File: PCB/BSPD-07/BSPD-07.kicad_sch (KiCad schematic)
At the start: 54 parts, among them IC1 LM393LVQDRQ1, IC2 LM393LVQDRQ1, IC3 LM393LVQDRQ1, IC4 LDO40LPU50RY, IC5 74LVC1G02GW-Q100H, J1 DTM13-12PA, Q1 RSQ025P03HZGTR, Q2 RJU002N06FRAT106, Q3 RJU002N06FRAT106, U2 TLP175A / COMUS AB38-Q

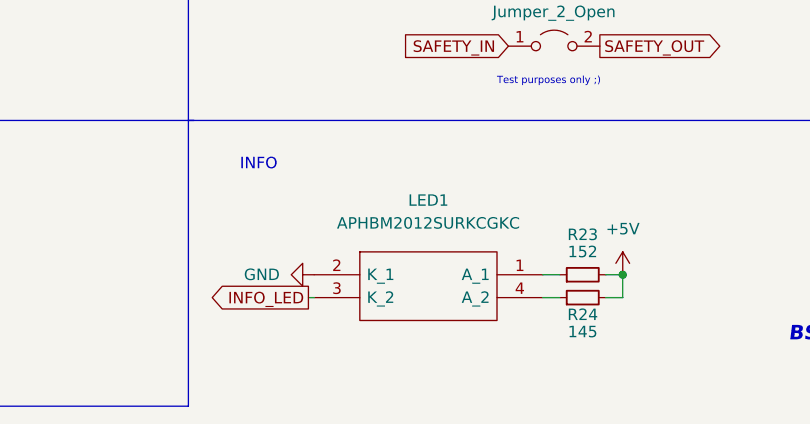
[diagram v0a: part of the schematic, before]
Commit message: Layout rework + led change
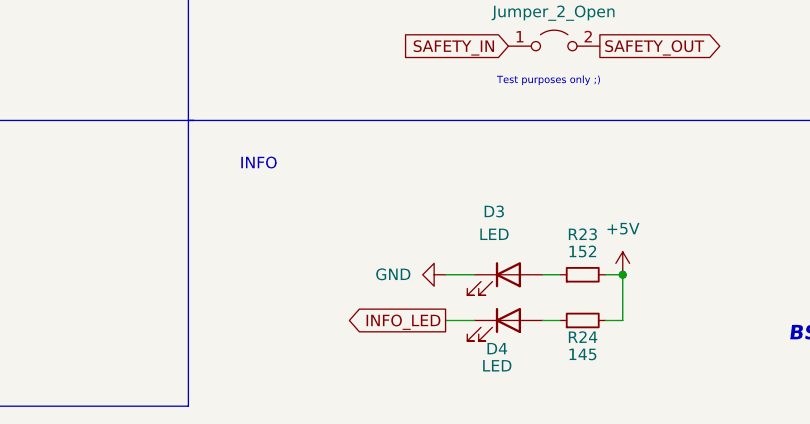
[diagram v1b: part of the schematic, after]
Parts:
- removed LED1: APHBM2012SURKCGKC, BSPD_07:APHBM2012SURKCGKC, symbol BSPD-07:APHBM2012SURKCGKC
- added D3, D4: LED, Diode_SMD:D_0402_1005Metric_Pad0.77x0.64mm_HandSolder, symbol Device:LED
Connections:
- net GND: now also D3.1 (K)
- net INFO_LED: now also D4.1 (K)
- net at R24.1: now also D4.2 (A)
- net at R23.1: now also D3.2 (A)
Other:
- moved on the sheet: R24
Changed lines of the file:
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@@
+    (stroke (width 0) (type default) (color 0 0 0 0))
+  )
+  (wire (pts (xy 159.385 188.595) (xy 161.29 188.595))
     (stroke (width 0) (type default) (color 0 0 0 0))
   )
@@
     (stroke (width 0) (type default) (color 0 0 0 0))
   )
-  (wire (pts (xy 159.385 186.055) (xy 161.29 186.055))
-    (stroke (width 0) (type default) (color 0 0 0 0))
-  )
   (polyline (pts (xy 193.675 52.705) (xy 150.495 52.705))
     (stroke (width 0) (type default) (color 0 0 0 0))
@@
     (stroke (width 0) (type default) (color 0 0 0 0))
   )
+  (wire (pts (xy 148.59 188.595) (xy 151.765 188.595))
+    (stroke (width 0) (type default) (color 0 0 0 0))
+  )
   (wire (pts (xy 159.385 139.065) (xy 159.385 140.335))
     (stroke (width 0) (type default) (color 0 0 0 0))
@@
     (stroke (width 0) (type default) (color 0 0 0 0))
   )
-  (wire (pts (xy 133.35 186.055) (xy 133.985 186.055))
-    (stroke (width 0) (type default) (color 0 0 0 0))
-  )
   (wire (pts (xy 57.785 107.95) (xy 59.69 107.95))
     (stroke (width 0) (type default) (color 0 0 0 0))
@@
     (stroke (width 0) (type default) (color 0 0 0 0))
   )
+  (wire (pts (xy 168.275 188.595) (xy 166.37 188.595))
+    (stroke (width 0) (type default) (color 0 0 0 0))
+  )
   (wire (pts (xy 263.525 120.65) (xy 263.525 123.19))
     (stroke (width 0) (type default) (color 0 0 0 0))
@@
     (stroke (width 0) (type default) (color 0 0 0 0))
   )
-  (wire (pts (xy 168.275 186.055) (xy 168.275 183.515))
+  (wire (pts (xy 168.275 183.515) (xy 168.275 188.595))
     (stroke (width 0) (type default) (color 0 0 0 0))
   )
@@
     (stroke (width 0) (type default) (color 0 0 0 0))
   )
+  (wire (pts (xy 148.59 183.515) (xy 151.765 183.515))
+    (stroke (width 0) (type default) (color 0 0 0 0))
+  )
   (wire (pts (xy 50.8 33.02) (xy 50.8 38.1))
     (stroke (width 0) (type default) (color 0 0 0 0))
@@
   )
   (wire (pts (xy 220.98 47.625) (xy 220.98 52.07))
-    (stroke (width 0) (type default) (color 0 0 0 0))
-  )
-  (wire (pts (xy 166.37 186.055) (xy 168.275 186.055))
     (stroke (width 0) (type default) (color 0 0 0 0))
   )
@@
     )
   )
-  (global_label "INFO_LED" (shape output) (at 133.35 186.055 180) (fields_autoplaced)
+  (global_label "INFO_LED" (shape output) (at 148.59 188.595 180) (fields_autoplaced)
     (effects (font (size 1.27 1.27)) (justify right))
-    (property "Intersheet References" "${INTERSHEET_REFS}" (id 0) (at 122.1679 185.9756 0)
+    (property "Intersheet References" "${INTERSHEET_REFS}" (id 0) (at 137.4079 188.5156 0)
       (effects (font (size 1.27 1.27)) (justify right) hide)
     )
@@
     (pin "1")
   )
-  (symbol (lib_id "Device:R_Small") (at 163.83 186.055 90) (unit 1)
-    (in_bom yes) (on_board yes)
-    (property "Reference" "R24" (id 0) (at 163.83 187.96 90))
-    (property "Value" "145" (id 1) (at 163.83 189.865 90))
-    (property "Footprint" "Resistor_SMD:R_0402_1005Metric" (id 2) (at 163.83 186.055 0)
-      (effects (font (size 1.27 1.27)) hide)
-    )
-    (property "Datasheet" "~" (id 3) (at 163.83 186.055 0)
+  (symbol (lib_id "Device:R_Small") (at 163.83 188.595 90) (unit 1)
+    (in_bom yes) (on_board yes)
+    (property "Reference" "R24" (id 0) (at 163.83 190.5 90))
+    (property "Value" "145" (id 1) (at 163.83 192.405 90))
+    (property "Footprint" "Resistor_SMD:R_0402_1005Metric" (id 2) (at 163.83 188.595 0)
+      (effects (font (size 1.27 1.27)) hide)
+    )
+    (property "Datasheet" "~" (id 3) (at 163.83 188.595 0)
       (effects (font (size 1.27 1.27)) hide)
     )
@@
     (pin "1")
     (pin "2")
-  )
-  (symbol (lib_id "BSPD-07:APHBM2012SURKCGKC") (at 133.985 183.515 0) (unit 1)
-    (in_bom yes) (on_board yes) (fields_autoplaced)
-    (property "Reference" "LED1" (id 0) (at 146.685 175.26 0))
-    (property "Value" "APHBM2012SURKCGKC" (id 1) (at 146.685 177.8 0))
-    (property "Footprint" "BSPD_07:APHBM2012SURKCGKC" (id 2) (at 155.575 180.975 0)
-      (effects (font (size 1.27 1.27)) (justify left) hide)
-    )
-    (property "Datasheet" "https://mouser.componentsearchengine.com/Datasheets/3/APHBM2012SURKCGKC.pdf" (id 3) (at 155.575 183.515 0)
-      (effects (font (size 1.27 1.27)) (justify left) hide)
-    )
-    (property "Description" "2.0X1.2MM RED/GREEN SMD LED Kingbright APHBM2012SURKCGKC, APHBM2012 Series Bi-colour Green, Red LED, 570 / 630 nm 4-Pin 2012 (0805) Clear" (id 4) (at 155.575 186.055 0)
-      (effects (font (size 1.27 1.27)) (justify left) hide)
-    )
-    (property "Height" "0.45" (id 5) (at 155.575 188.595 0)
-      (effects (font (size 1.27 1.27)) (justify left) hide)
-    )
-    (property "Manufacturer_Name" "Kingbright" (id 6) (at 155.575 191.135 0)
-      (effects (font (size 1.27 1.27)) (justify left) hide)
-    )
-    (property "Manufacturer_Part_Number" "APHBM2012SURKCGKC" (id 7) (at 155.575 193.675 0)
-      (effects (font (size 1.27 1.27)) (justify left) hide)
-    )
-    (property "Mouser Part Number" "604-BM2012SURKCGKC" (id 8) (at 155.575 196.215 0)
-      (effects (font (size 1.27 1.27)) (justify left) hide)
-    )
-    (property "Mouser Price/Stock" "https://www.mouser.co.uk/ProductDetail/Kingbright/APHBM2012SURKCGKC?qs=mWUXtl%252BhaIKZSpp3TSJ%2FQA%3D%3D" (id 9) (at 155.575 198.755 0)
-      (effects (font (size 1.27 1.27)) (justify left) hide)
-    )
-    (property "Arrow Part Number" "APHBM2012SURKCGKC" (id 10) (at 155.575 201.295 0)
-      (effects (font (size 1.27 1.27)) (justify left) hide)
-    )
-    (property "Arrow Price/Stock" "https://www.arrow.com/en/products/aphbm2012surkcgkc/kingbright?region=nac" (id 11) (at 155.575 203.835 0)
-      (effects (font (size 1.27 1.27)) (justify left) hide)
-    )
-    (property "Mouser Testing Part Number" "" (id 12) (at 155.575 206.375 0)
-      (effects (font (size 1.27 1.27)) (justify left) hide)
-    )
-    (property "Mouser Testing Price/Stock" "" (id 13) (at 155.575 208.915 0)
-      (effects (font (size 1.27 1.27)) (justify left) hide)
-    )
-    (pin "1")
-    (pin "2")
-    (pin "3")
-    (pin "4")
   )
   (symbol (lib_id "power:+5V") (at 213.995 36.195 270) (unit 1)
@@
     (pin "3")
   )
+  (symbol (lib_id "Device:LED") (at 155.575 188.595 0) (unit 1)
+    (in_bom yes) (on_board yes)
+    (property "Reference" "D4" (id 0) (at 154.305 191.77 0))
+    (property "Value" "LED" (id 1) (at 154.305 193.675 0))
+    (property "Footprint" "Diode_SMD:D_0402_1005Metric_Pad0.77x0.64mm_HandSolder" (id 2) (at 155.575 188.595 0)
+      (effects (font (size 1.27 1.27)) hide)
+    )
+    (property "Datasheet" "~" (id 3) (at 155.575 188.595 0)
+      (effects (font (size 1.27 1.27)) hide)
+    )
+    (pin "1")
+    (pin "2")
+  )
   (symbol (lib_id "BSPD-07:74LVC1G02GW-Q100H") (at 49.53 146.05 0) (unit 1)
     (in_bom yes) (on_board yes) (fields_autoplaced)
@@
     (pin "1")
   )
-  (symbol (lib_id "power:GND") (at 133.985 183.515 270) (unit 1)
-    (in_bom yes) (on_board yes) (fields_autoplaced)
-    (property "Reference" "#PWR0147" (id 0) (at 127.635 183.515 0)
-      (effects (font (size 1.27 1.27)) hide)
-    )
-    (property "Value" "GND" (id 1) (at 130.175 183.5149 90)
+  (symbol (lib_id "power:GND") (at 148.59 183.515 270) (unit 1)
+    (in_bom yes) (on_board yes) (fields_autoplaced)
+    (property "Reference" "#PWR0147" (id 0) (at 142.24 183.515 0)
+      (effects (font (size 1.27 1.27)) hide)
+    )
+    (property "Value" "GND" (id 1) (at 144.78 183.5149 90)
       (effects (font (size 1.27 1.27)) (justify right))
     )
-    (property "Footprint" "" (id 2) (at 133.985 183.515 0)
-      (effects (font (size 1.27 1.27)) hide)
-    )
-    (property "Datasheet" "" (id 3) (at 133.985 183.515 0)
+    (property "Footprint" "" (id 2) (at 148.59 183.515 0)
+      (effects (font (size 1.27 1.27)) hide)
+    )
+    (property "Datasheet" "" (id 3) (at 148.59 183.515 0)
       (effects (font (size 1.27 1.27)) hide)
     )
@@
     (pin "2")
   )
+  (symbol (lib_id "Device:LED") (at 155.575 183.515 0) (unit 1)
+    (in_bom yes) (on_board yes) (fields_autoplaced)
+    (property "Reference" "D3" (id 0) (at 153.9875 176.53 0))
+    (property "Value" "LED" (id 1) (at 153.9875 179.07 0))
+    (property "Footprint" "Diode_SMD:D_0402_1005Metric_Pad0.77x0.64mm_HandSolder" (id 2) (at 155.575 183.515 0)
+      (effects (font (size 1.27 1.27)) hide)
+    )
+    (property "Datasheet" "~" (id 3) (at 155.575 183.515 0)
+      (effects (font (size 1.27 1.27)) hide)
+    )
+    (pin "1")
+    (pin "2")
+  )
   (symbol (lib_id "Device:R_Small") (at 218.44 50.8 0) (unit 1)
     (in_bom yes) (on_board yes)
@@
       (reference "D2") (unit 1) (value "7V") (footprint "Diode_SMD:D_0402_1005Metric")
     )
+    (path "/ceeae0f3-eeb4-4e60-9d26-30190a673d37"
+      (reference "D3") (unit 1) (value "LED") (footprint "Diode_SMD:D_0402_1005Metric_Pad0.77x0.64mm_HandSolder")
+    )
+    (path "/8f4dccc8-5830-44b2-a241-6731b10d74d3"
+      (reference "D4") (unit 1) (value "LED") (footprint "Diode_SMD:D_0402_1005Metric_Pad0.77x0.64mm_HandSolder")
+    )
     (path "/90a442e5-8955-4be7-a2a2-5ce96ee123ec"
       (reference "IC1") (unit 1) (value "LM393LVQDRQ1") (footprint "BSPD_07:SOIC127P600X175-8N")
@@
       (reference "JP1") (unit 1) (value "Jumper_2_Open") (footprint "Connector_PinHeader_2.54mm:PinHeader_1x02_P2.54mm_Vertical")
     )
-    (path "/483773a8-f535-4c4a-b59c-54e2d7943e4d"
-      (reference "LED1") (unit 1) (value "APHBM2012SURKCGKC") (footprint "BSPD_07:APHBM2012SURKCGKC")
-    )
     (path "/a5696659-0be2-4e22-8039-65953ee49bcb"

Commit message: Revised layout
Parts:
- added Q4: AO3401A, Package_TO_SOT_SMD:SOT-23, symbol Transistor_FET:AO3401A
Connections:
- net +12V: now also Q4.3 (D); no longer C6.1, IC4.2 (EN), IC4.3 (VIN)
- net GND: now also Q4.1 (G)
- new net: C6.1, IC4.2 (EN), IC4.3 (VIN), Q4.2 (S)
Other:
- moved on the sheet: C6, C7, IC4

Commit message: Final version with gerbers generated
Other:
- note added: "10S DELAY"
- note added: "<- Currently 1.1M"
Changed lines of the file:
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@@
+    (stroke (width 0) (type default) (color 0 0 0 0))
+  )
+  (polyline (pts (xy 257.81 44.45) (xy 257.81 77.47))
     (stroke (width 0) (type default) (color 0 0 0 0))
   )
@@
     (stroke (width 0) (type default) (color 0 0 0 0))
   )
-  (polyline (pts (xy 200.66 92.71) (xy 251.46 92.71))
+  (polyline (pts (xy 200.66 93.98) (xy 251.46 93.98))
     (stroke (width 0) (type default) (color 0 0 0 0))
   )
@@
     (stroke (width 0) (type default) (color 0 0 0 0))
   )
-  (polyline (pts (xy 251.46 92.71) (xy 251.46 64.77))
+  (polyline (pts (xy 251.46 93.98) (xy 251.46 64.77))
     (stroke (width 0) (type default) (color 0 0 0 0))
   )
@@
     (stroke (width 0) (type default) (color 0 0 0 0))
   )
+  (polyline (pts (xy 257.81 44.45) (xy 270.51 44.45))
+    (stroke (width 0) (type default) (color 0 0 0 0))
+  )
   (wire (pts (xy 55.245 28.575) (xy 55.245 30.48))
     (stroke (width 0) (type default) (color 0 0 0 0))
@@
     (stroke (width 0) (type default) (color 0 0 0 0))
   )
+  (polyline (pts (xy 270.51 77.47) (xy 257.81 77.47))
+    (stroke (width 0) (type default) (color 0 0 0 0))
+  )
   (wire (pts (xy 87.63 41.91) (xy 90.17 41.91))
     (stroke (width 0) (type default) (color 0 0 0 0))
   )
-  (polyline (pts (xy 200.66 64.77) (xy 200.66 92.71))
+  (polyline (pts (xy 200.66 64.77) (xy 200.66 93.98))
     (stroke (width 0) (type default) (color 0 0 0 0))
   )
@@
   )
   (wire (pts (xy 41.91 40.64) (xy 41.91 41.91))
+    (stroke (width 0) (type default) (color 0 0 0 0))
+  )
+  (polyline (pts (xy 270.51 44.45) (xy 270.51 77.47))
     (stroke (width 0) (type default) (color 0 0 0 0))
   )
@@
     (effects (font (size 0.8 0.8)) (justify left bottom))
   )
+  (text "10S DELAY" (at 260.35 44.45 0)
+    (effects (font (size 1.27 1.27)) (justify left bottom))
+  )
   (text "HEADER" (at 19.05 171.45 0)
     (effects (font (size 1.8 1.8)) (justify left bottom))
@@
     (effects (font (size 1.6 1.6)) (justify left bottom))
   )
+  (text "<- Currently 1.1M" (at 274.32 68.58 0)
+    (effects (font (size 1.27 1.27)) (justify left bottom))
+  )
   (text "BSPD for PGR-07 (2023)" (at 186.69 191.135 0)

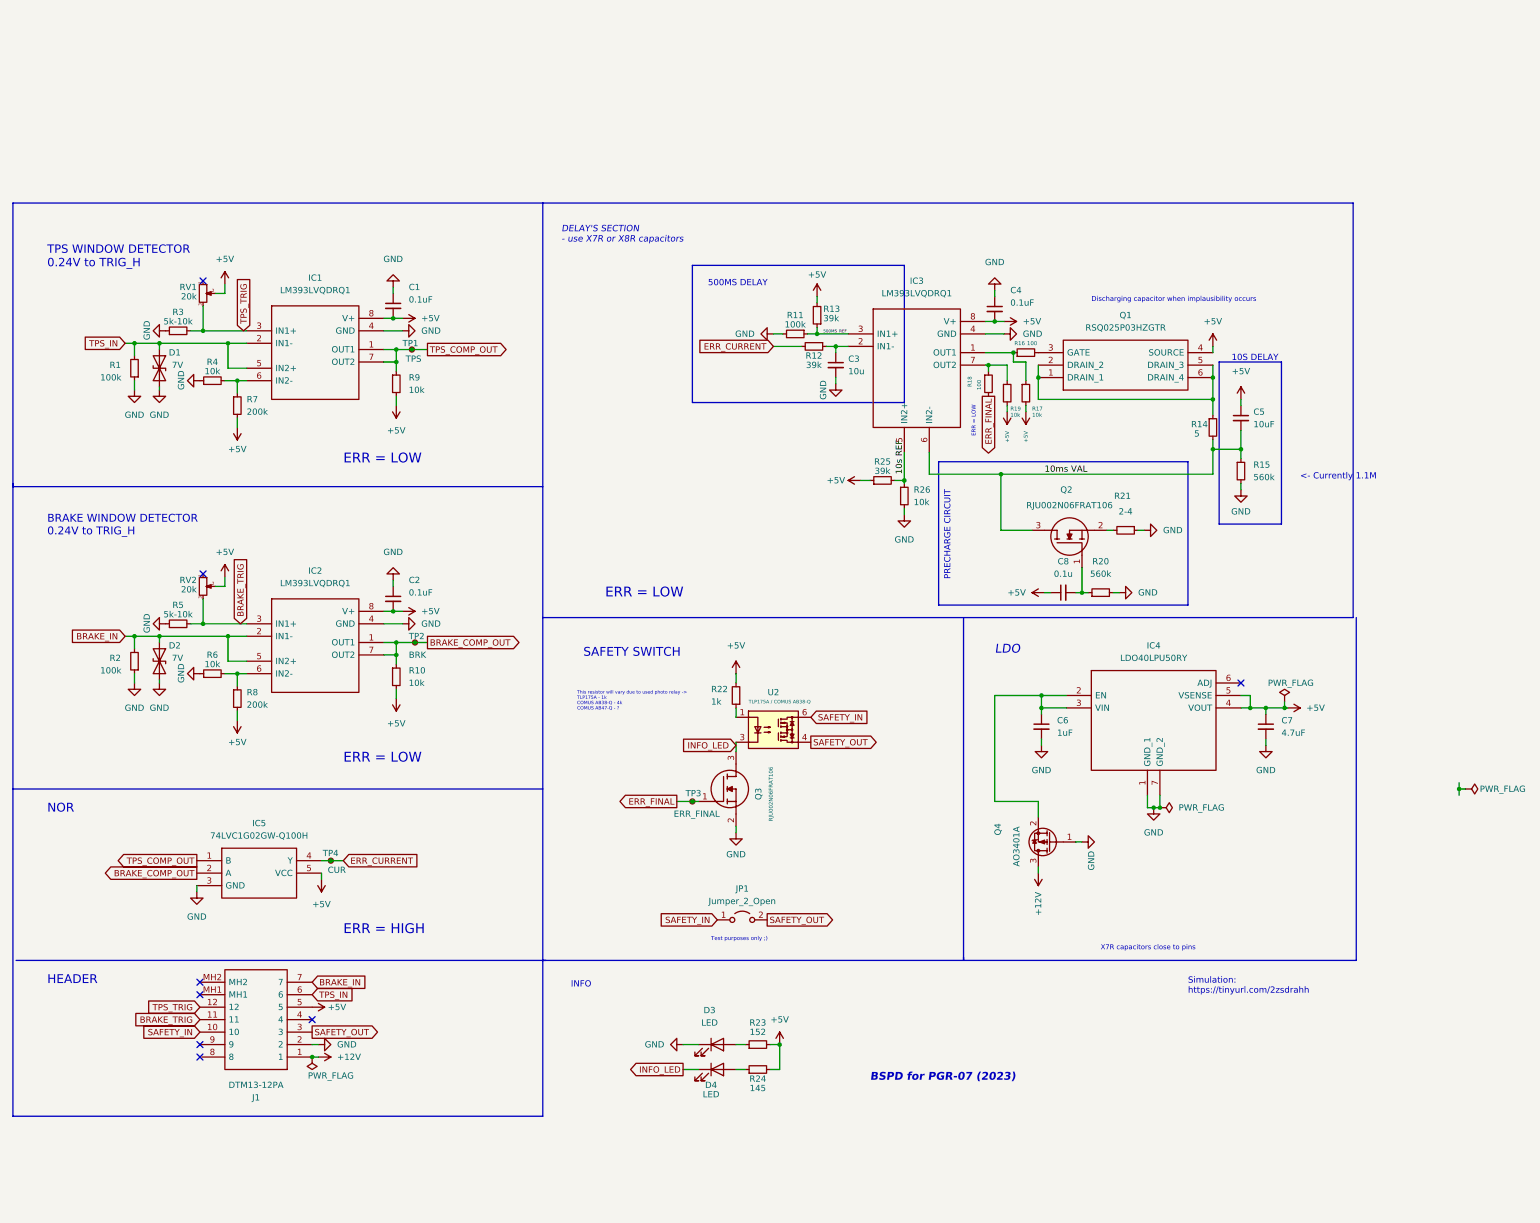
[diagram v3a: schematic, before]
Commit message: Added SCS compliant solution ver 1.0
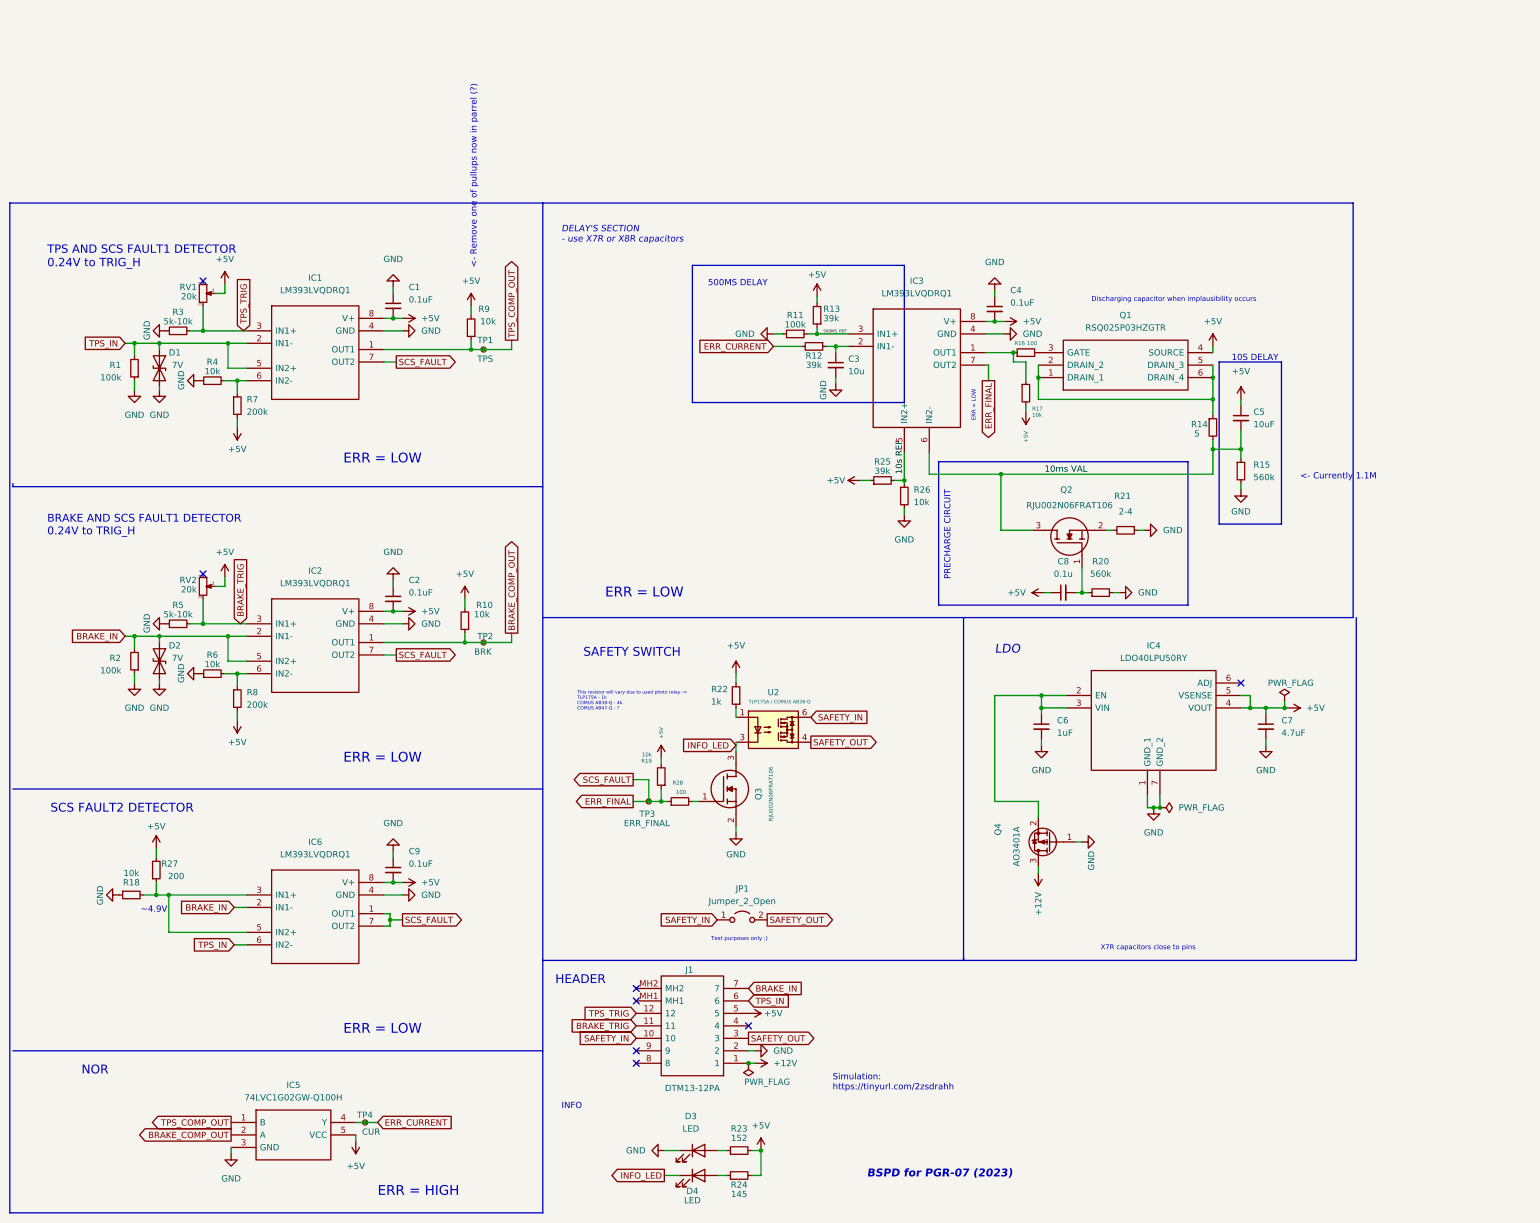
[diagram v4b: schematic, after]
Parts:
- added C9: 0.1uF, Capacitor_SMD:C_0402_1005Metric, symbol Device:C_Small
- added IC6: LM393LVQDRQ1, BSPD_07:SOIC127P600X175-8N, symbol BSPD-07:LM393LVQDRQ1
- added R27: 200, Resistor_SMD:R_0402_1005Metric, symbol Device:R_Small
- added R28: 100, Resistor_SMD:R_0402_1005Metric, symbol Device:R_Small
- R18: value 100 -> 10k
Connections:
- net +5V: now also C9.2, IC6.8 (V+), R27.2
- net BRAKE_COMP_OUT: no longer IC2.7 (OUT2)
- net BRAKE_IN: now also IC6.2 (IN1-)
- net ERR_FINAL: now also IC1.7 (OUT2), IC2.7 (OUT2), IC3.7 (OUT2), R19.1, IC6.1 (OUT1), IC6.7 (OUT2), R28.1; no longer Q3.1, R18.2
- net GND: now also R18.1, C9.1, IC6.4 (GND)
- net TPS_COMP_OUT: no longer IC1.7 (OUT2)
- net TPS_IN: now also IC6.6 (IN2-)
- new net: IC6.3 (IN1+), IC6.5 (IN2+), R18.2, R27.1
- new net: Q3.1, R28.2
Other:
- note added: "<- Remove one of pullups now in parrel (?)"
- note added: "BRAKE AND SCS FAULT1 DETECTOR 0.24V to TRIG_H"
- note added: "SCS FAULT2 DETECTOR"
- note added: "TPS AND SCS FAULT1 DETECTOR 0.24V to TRIG_H"
- note added: "~4.9V"
- note removed: "BRAKE WINDOW DETECTOR 0.24V to TRIG_H"
- note removed: "TPS WINDOW DETECTOR 0.24V to TRIG_H"
- moved on the sheet: D3, D4, IC5, J1, R10, R19, R23, R24, R9, TP1, TP2, TP3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
